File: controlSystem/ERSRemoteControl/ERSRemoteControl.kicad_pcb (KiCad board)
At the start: 2 copper layers, 58.8 x 37.7 mm, 58 parts, among them J1 USB_C_Receptacle_USB2.0_14P, J2 0022-232041, J3 Conn_01x06, J4 00222-32051, J5 0022-232021, J6 0022-232021, SW1 SW_SPDT, SW2 SW_Push, SW3 SW_Push, SW4 SW_Push, SW5 SW_Push, SW6 SW_Push, SW7 SW_Push, U1 TPS63070, U2 ESP32-S3-WROOM-1, U3 TCAN330

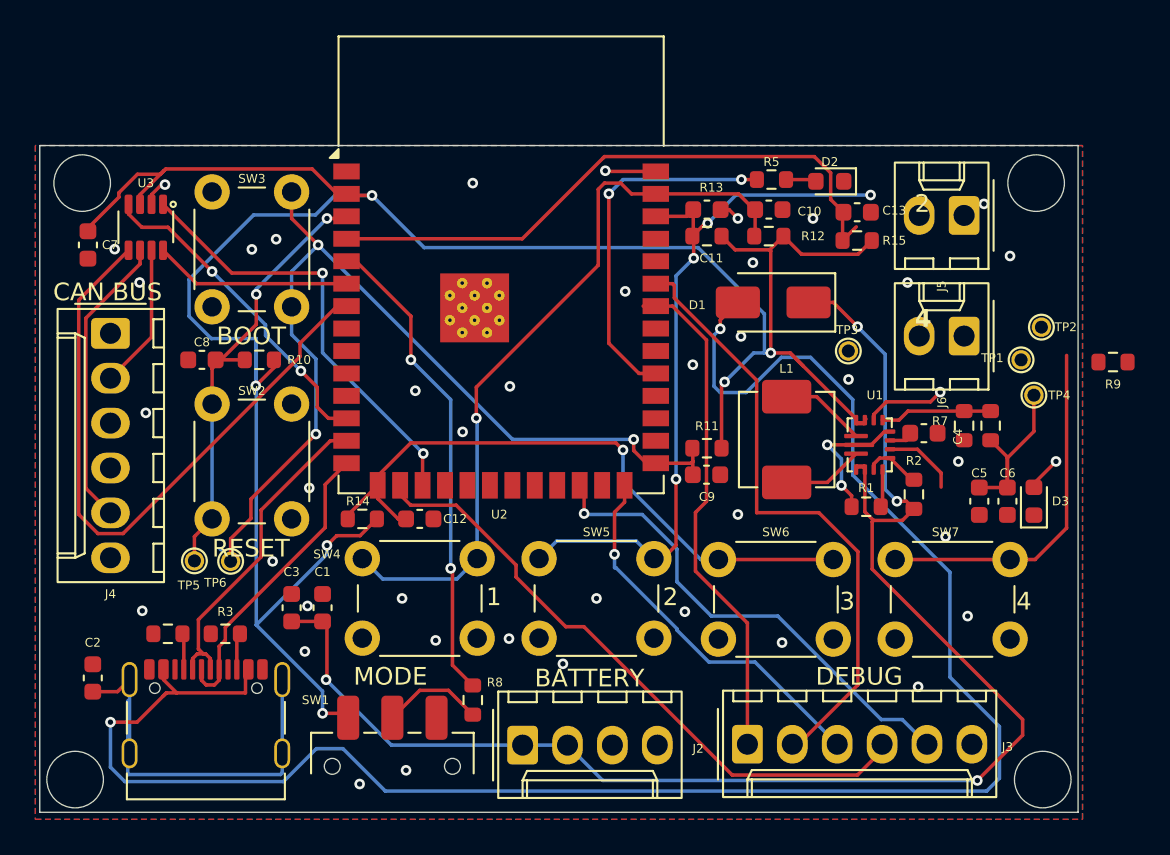
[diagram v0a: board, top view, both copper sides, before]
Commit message: Fixed missing reference designators
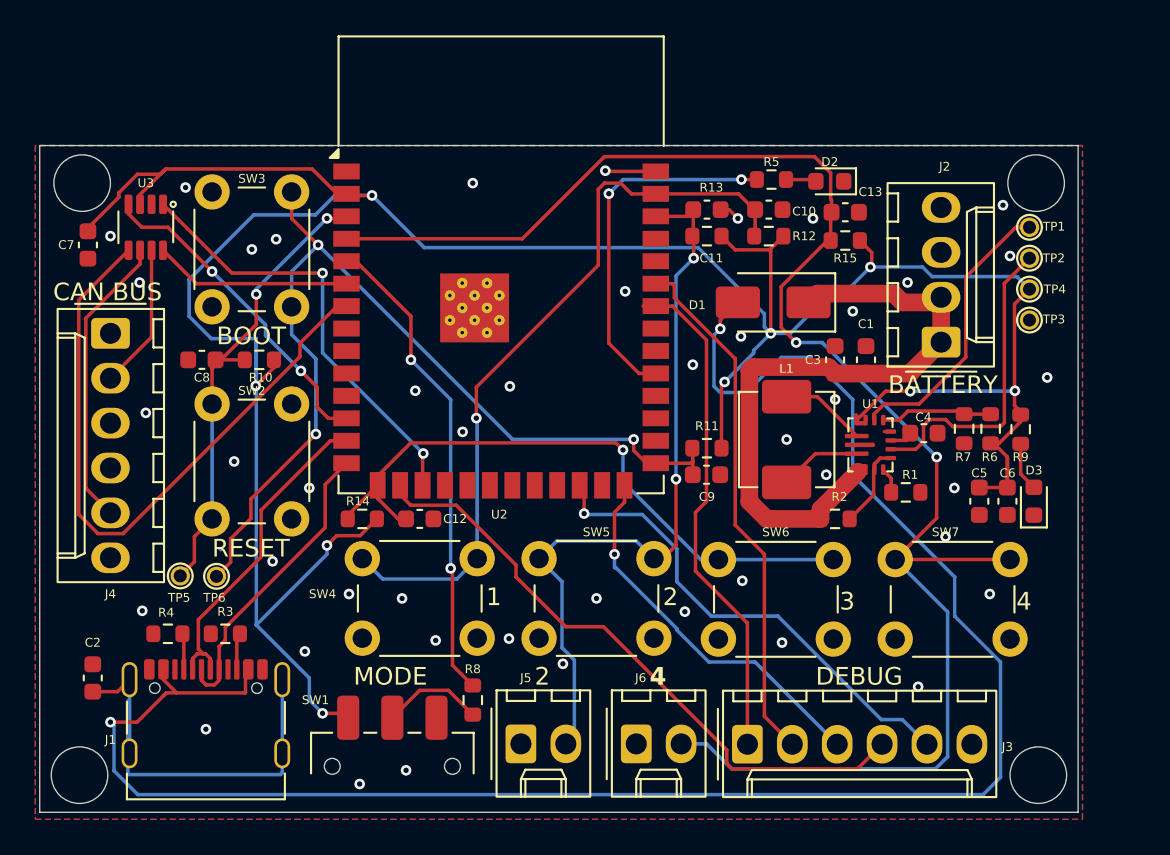
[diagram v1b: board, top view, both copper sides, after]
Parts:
- moved J5 39.0 mm to (101.2, 124.7), turned to 0 degrees
- moved C1 33.8 mm to (120.8, 103.0)
- moved C3 33.8 mm to (119.0, 103.0)
- moved J2 32.9 mm to (125.0, 102.0), turned to 90 degrees
- moved J6 29.6 mm to (107.8, 124.7), turned to 0 degrees
- moved TP3 10.4 mm to (130.0, 100.8)
- moved TP1 7.52 mm to (130.0, 95.5)
- moved R9 6.46 mm to (129.5, 106.9), turned to -90 degrees
- moved TP4 6.01 mm to (130.0, 99.0)
- moved R2 4.67 mm to (119.0, 112.0), turned to 0 degrees
- moved TP2 3.96 mm to (130.0, 97.2)
- moved R1 2.38 mm to (123.0, 110.5), turned to 0 degrees
- moved TP5 1.17 mm to (82.0, 115.2)
- moved TP6 1.17 mm to (84.0, 115.2)
- moved C13 0.67 mm to (119.6, 94.7)
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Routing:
- net Net-(D1-K): track 85.2 -> 37.8 mm, vias 4 -> 0
- net /SWITCH 4: track 55.9 -> 94.0 mm, vias 0 -> 2
- net +3.3V: track 147.0 -> 166.6 mm, vias 6 -> 9
- net Net-(U1-PG): track 4.25 -> 17.8 mm
- net Net-(U1-FB2): track 4.61 -> 16.2 mm, vias 1 -> 0
- net GND: track 14.6 -> 5.57 mm, vias 42 -> 45
- net Net-(J3-Pin_2): track 35.2 -> 30.2 mm
- net Net-(U1-EN): track 3.24 -> 4.75 mm
- net +5V: track 107.0 -> 105.7 mm
- net /BOOT: track 53.2 -> 54.4 mm
- net /RESET: track 26.7 -> 27.9 mm
- net /SWITCH 2: track 41.7 -> 42.8 mm, vias 4 -> 2
- net Net-(D3-A): track 1.98 -> 2.99 mm, vias 1 -> 0
- net Net-(U1-VSEL): track 2.14 -> 1.48 mm

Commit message: Updated traces to .3 instead of .2
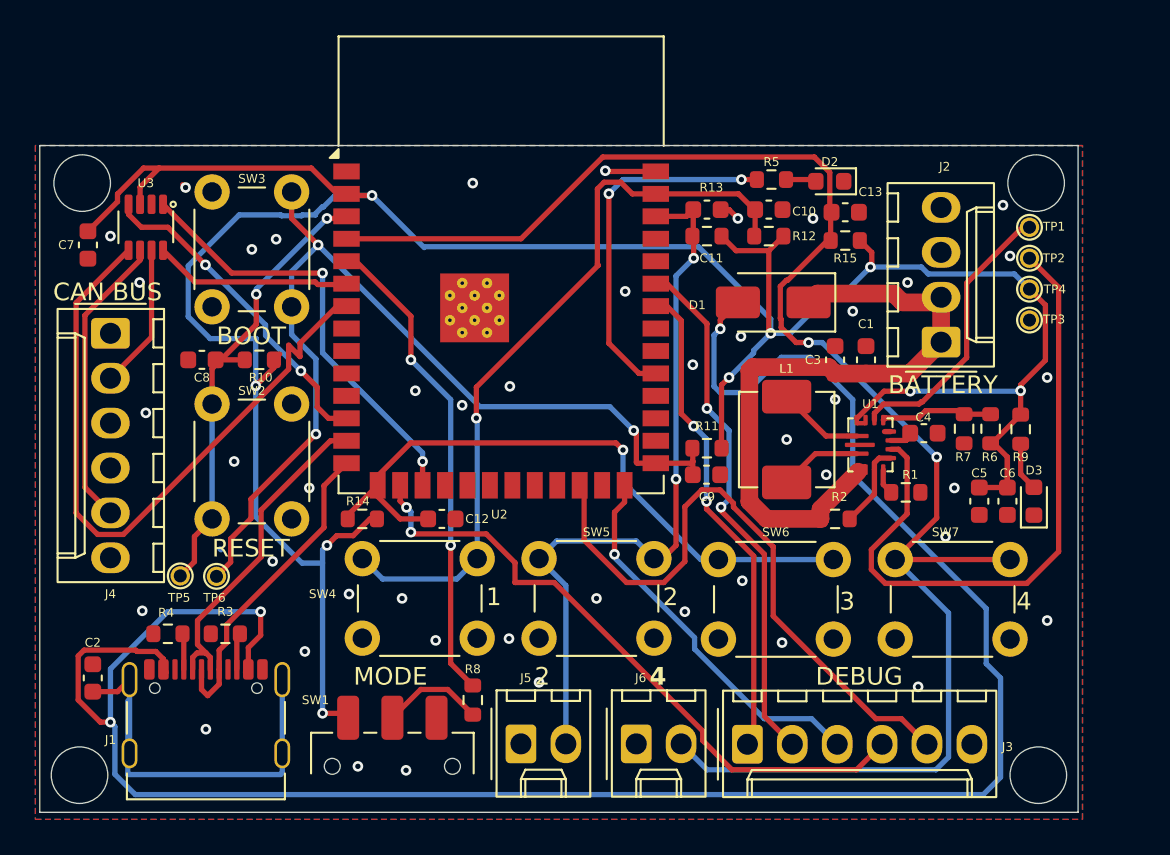
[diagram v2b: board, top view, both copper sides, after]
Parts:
- moved C12 1.25 mm to (96.8, 112.0)
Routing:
- net Net-(U1-PG): track 17.8 -> 37.2 mm
- net +5V: track 105.7 -> 121.4 mm, vias 2 -> 3
- net Net-(J3-Pin_5): track 27.6 -> 36.0 mm, vias 1 -> 0
- net +3.3V: track 166.6 -> 160.6 mm
- net Net-(U2-IO7): track 37.5 -> 39.0 mm
- net /SWITCH 3: track 36.3 -> 37.5 mm
- net Net-(J3-Pin_1): track 28.7 -> 27.6 mm, vias 0 -> 2
- net Net-(J3-Pin_4): track 36.0 -> 37.1 mm, vias 0 -> 2
- net Net-(U2-USB_D+): track 17.1 -> 18.0 mm
- net /BOOT: track 54.4 -> 55.0 mm
- net Net-(J3-Pin_2): track 30.2 -> 30.4 mm, vias 0 -> 2

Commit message: Minor trace updates
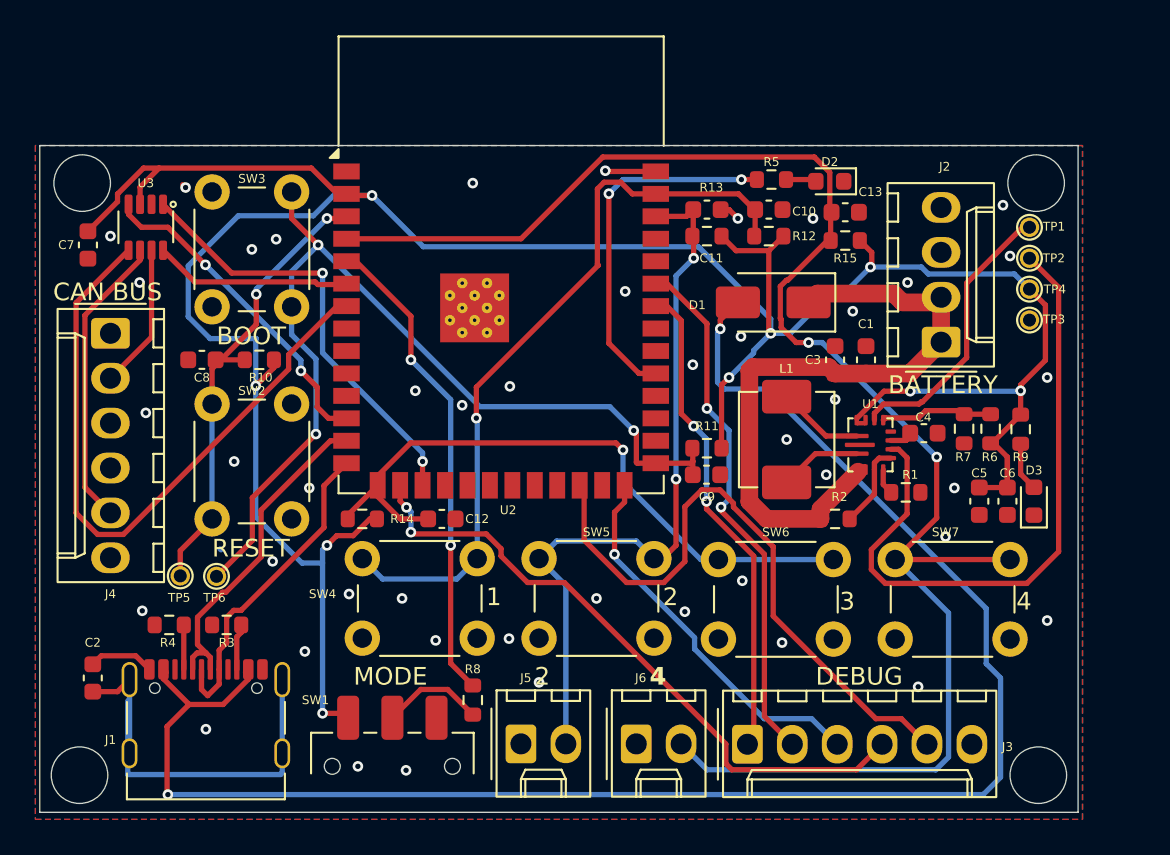
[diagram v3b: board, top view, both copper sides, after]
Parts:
- moved R3 0.51 mm to (84.6, 118.0)
- moved R4 0.51 mm to (81.3, 118.0)
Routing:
- net +5V: track 121.4 -> 96.1 mm, vias 3 -> 2
- net GND: track 5.57 -> 8.93 mm
- net Net-(U2-IO7): track 39.0 -> 37.7 mm
- net Net-(J1-CC2): track 2.09 -> 2.62 mm

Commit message: Removed CAN stuff and replaced with serial
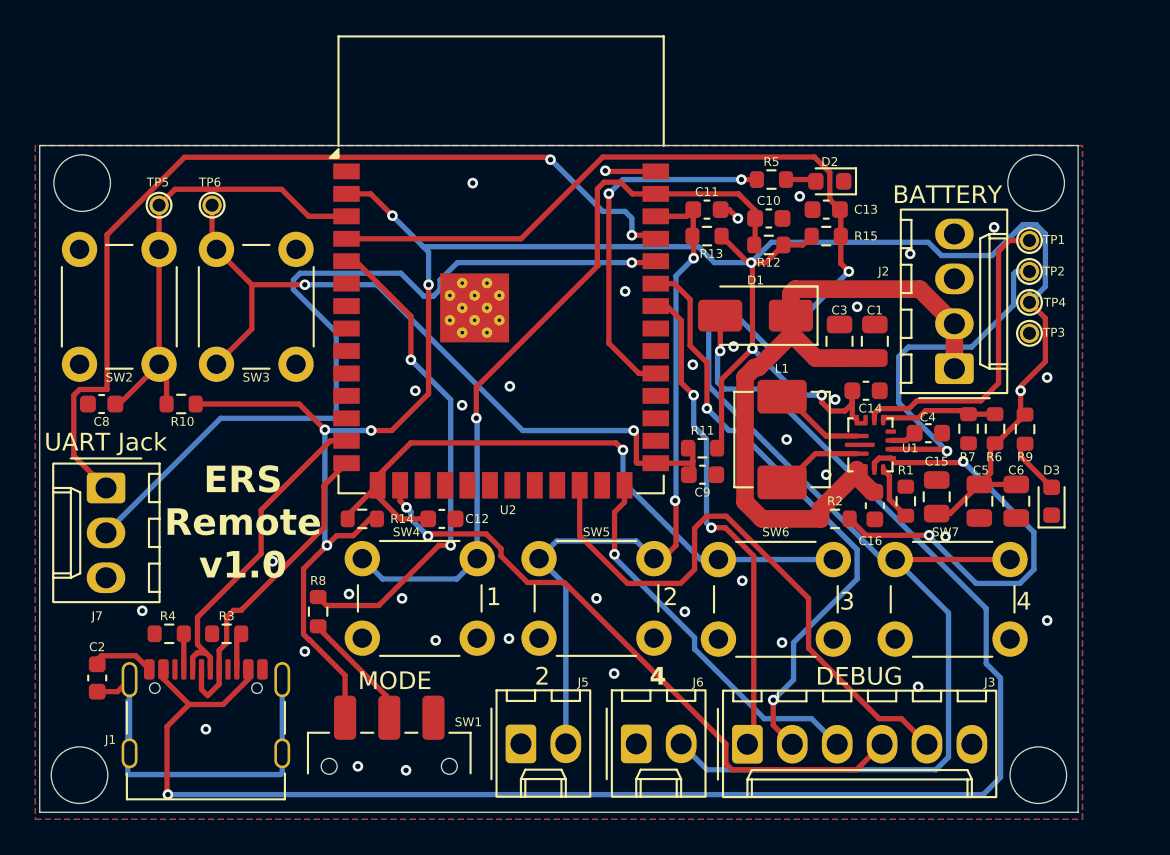
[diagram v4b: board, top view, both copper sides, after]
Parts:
- removed C7: 100n, Capacitor_SMD:C_0603_1608Metric
- removed J4: 00222-32051, Connector_Molex:Molex_KK-254_AE-6410-06A_1x06_P2.54mm_Vertical
- removed U3: TCAN330, psas-footprints:SOT23-8
- added C14: 10u, Capacitor_SMD:C_0603_1608Metric, F.Cu at (120.8, 104.8)
- added C15: 22u, Capacitor_SMD:C_0805_2012Metric, F.Cu at (124.8, 110.8)
- added C16: 10u, Capacitor_SMD:C_0603_1608Metric, F.Cu at (121.2, 111.2)
- added J7: 0022-232031, Connector_Molex:Molex_KK-254_AE-6410-03A_1x03_P2.54mm_Vertical, F.Cu at (77.8, 110.2)
- C1, C3, C5, C6: footprint Capacitor_SMD:C_0603_1608Metric -> Capacitor_SMD:C_0805_2012Metric
- J3: value Conn_01x06 -> 00222-32051
- R5: value 4.7 -> 4.7k
- moved TP5 21.0 mm to (80.8, 94.2)
- moved TP6 21.0 mm to (83.8, 94.2)
- moved SW2 15.5 mm to (80.8, 96.8), turned to -90 degrees
- moved SW3 10.6 mm to (84.0, 103.2), turned to 90 degrees
- moved R8 10.1 mm to (89.8, 117.2)
- moved C8 6.20 mm to (77.5, 105.5)
- moved R10 5.08 mm to (82.0, 105.5)
- moved J2 1.68 mm to (125.8, 103.5)
- moved D1 1.25 mm to (114.5, 100.5)
- moved C1 1.16 mm to (121.2, 102.0)
- moved R15 1.10 mm to (118.5, 96.0), turned to 0 degrees
- moved C13 1.09 mm to (118.5, 94.5), turned to 180 degrees
- moved C3 1.08 mm to (119.2, 102.0)
- moved D3 1.00 mm to (131.2, 111.0)
- moved TP1 0.75 mm to (130.0, 96.2)
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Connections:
- U2 pad 12: Net-(U2-IO8) -> unconnected-(U2-IO8-Pad12)
- U2 pad 17: Net-(U2-IO9) -> unconnected-(U2-IO9-Pad17)
- U2 pad 36: unconnected-(U2-RXD0-Pad36) -> Net-(J7-Pin_2)
- U2 pad 37: unconnected-(U2-TXD0-Pad37) -> Net-(J7-Pin_1)
- U2 pad 6: Net-(U2-IO6) -> unconnected-(U2-IO6-Pad6)
- U2 pad 7: Net-(U2-IO7) -> unconnected-(U2-IO7-Pad7)
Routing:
- net Net-(J7-Pin_1): track 0.00 -> 52.2 mm, vias 0 -> 2
- net Net-(J7-Pin_2): track 0.00 -> 46.9 mm, vias 0 -> 1
- net Net-(U2-IO7): track 37.7 -> 0.00 mm
- net Net-(U2-IO9): track 25.3 -> 0.00 mm, vias 2 -> 0
- net +3.3V: track 160.5 -> 139.0 mm
- net Net-(U1-EN): track 4.79 -> 25.7 mm, vias 0 -> 2
- net Net-(U2-IO8): track 18.7 -> 0.00 mm, vias 2 -> 0
- net Net-(U1-PG): track 37.2 -> 20.1 mm, vias 0 -> 1
- net Net-(J4-Pin_5): track 16.8 -> 0.00 mm
- net /BOOT: track 55.0 -> 42.7 mm, vias 3 -> 2
- net Net-(U2-IO6): track 11.2 -> 0.00 mm
- net Net-(J4-Pin_2): track 8.20 -> 0.00 mm
- net /SWITCH 4: track 94.1 -> 100.1 mm, vias 2 -> 1
- net Net-(J3-Pin_2): track 30.4 -> 34.5 mm
- net Net-(D1-K): track 37.8 -> 41.0 mm
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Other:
- board text added: "ERS Remote v1.0"
- board text added: "UART Jack"
- board text removed: "BOOT"
- board text removed: "CAN BUS"
- board text removed: "RESET"

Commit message: More changes to layout to make it cleaner
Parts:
- removed J3: 00222-32051, Connector_Molex:Molex_KK-254_AE-6410-06A_1x06_P2.54mm_Vertical
- added TP7: Test-Point, psas-footprints:TP-through-hole-1X01, F.Cu at (126.5, 92.0)
- added TP8: Test-Point, psas-footprints:TP-through-hole-1X01, F.Cu at (124.5, 92.0)
- moved J7 20.3 mm to (91.9, 124.8), turned to 0 degrees
- moved J6 15.3 mm to (123.0, 124.8)
- moved J5 14.0 mm to (115.2, 124.7)
- moved SW1 12.9 mm to (106.7, 125.0)
- moved C8 2.12 mm to (79.0, 107.0)
- moved R10 1.50 mm to (82.0, 107.0)
- moved SW2 1.00 mm to (80.8, 97.8)
- moved SW3 1.00 mm to (84.0, 104.2)
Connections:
- U2 pad 16: Net-(J3-Pin_4) -> unconnected-(U2-IO46-Pad16)
- U2 pad 24: Net-(J3-Pin_5) -> unconnected-(U2-IO47-Pad24)
- U2 pad 26: Net-(J3-Pin_3) -> unconnected-(U2-IO45-Pad26)
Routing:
- net Net-(J3-Pin_4): track 36.6 -> 0.00 mm, vias 2 -> 0
- net Net-(J3-Pin_5): track 33.9 -> 0.00 mm
- net Net-(J3-Pin_3): track 21.7 -> 0.00 mm, vias 1 -> 0
- net Net-(SW1-B): track 6.84 -> 26.5 mm
- net Net-(U2-IO42): track 34.5 -> 18.4 mm, vias 2 -> 1
- net Net-(J7-Pin_1): track 52.2 -> 37.0 mm
- net /SWITCH 2: track 43.1 -> 56.2 mm, vias 2 -> 1
- net Net-(J7-Pin_2): track 46.9 -> 36.7 mm, vias 1 -> 2
- net +3.3V: track 139.0 -> 146.7 mm, vias 9 -> 7
- net /SWITCH 4: track 100.1 -> 92.9 mm, vias 1 -> 0
- net Net-(U2-IO41): track 28.1 -> 20.9 mm, vias 2 -> 1
- net Net-(U1-PG): track 20.1 -> 15.4 mm, vias 1 -> 2
- net /RESET: track 27.4 -> 28.6 mm
- net Net-(U1-FB2): track 17.6 -> 16.9 mm, vias 0 -> 1
- net /BOOT: track 42.7 -> 42.4 mm, vias 2 -> 1
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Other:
- board text added: "BOOT"
- board text added: "RESET"
- board text removed: "DEBUG"

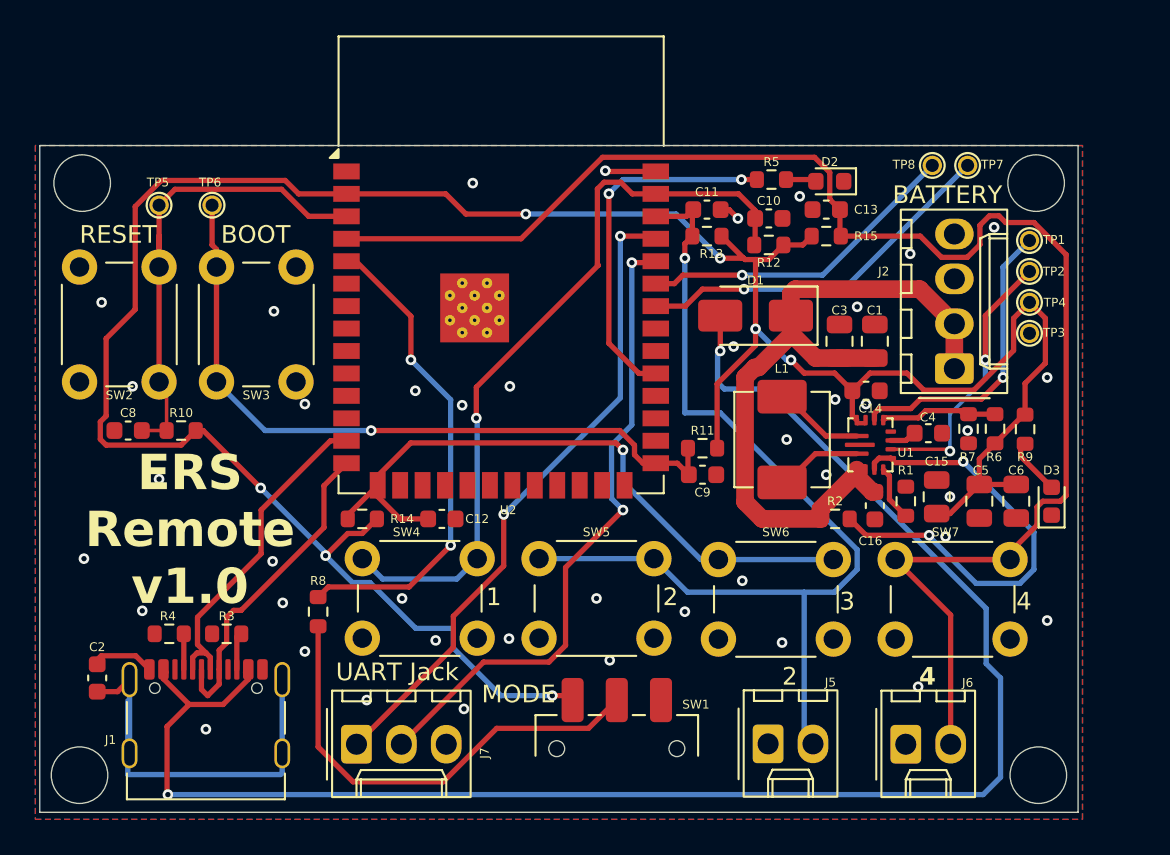
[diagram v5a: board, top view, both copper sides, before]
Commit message: Replaced components in BOM
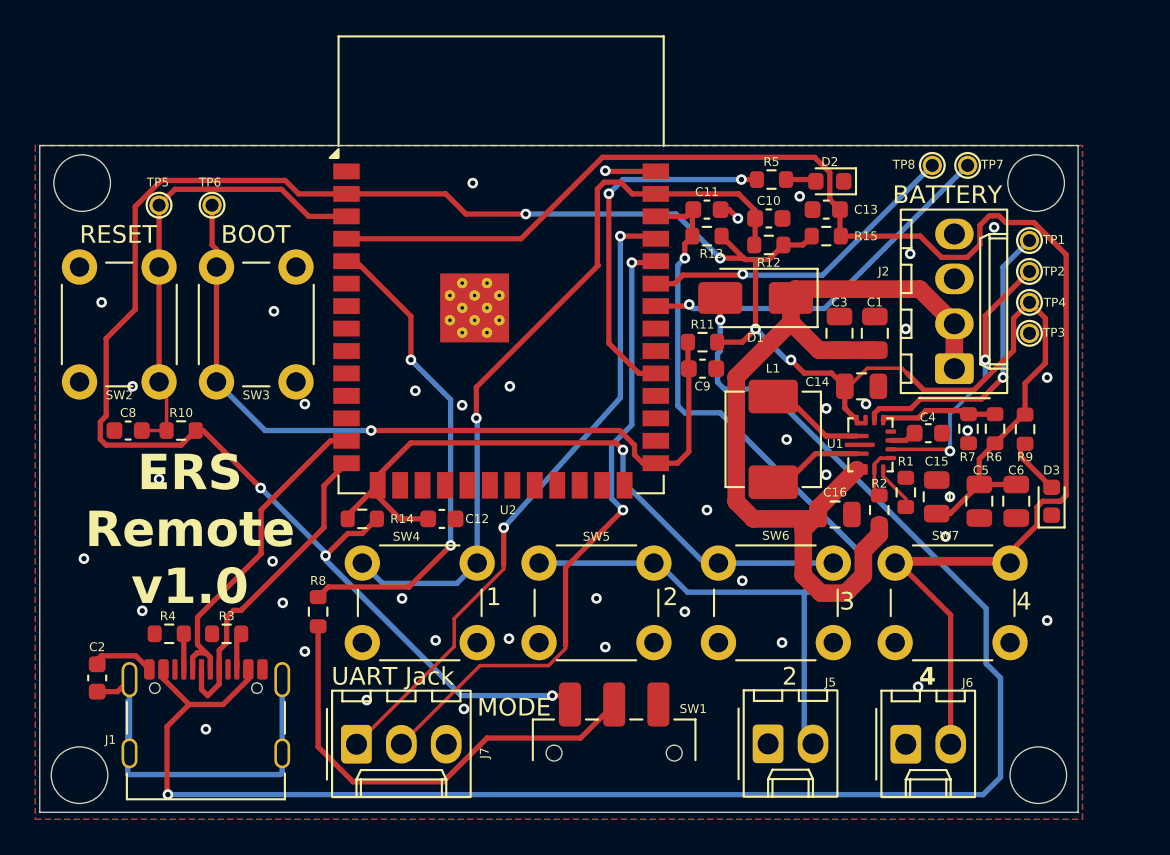
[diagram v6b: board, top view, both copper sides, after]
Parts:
- C14, C16: footprint Capacitor_SMD:C_0603_1608Metric -> Capacitor_SMD:C_0805_2012Metric
- moved C9 6.00 mm to (111.5, 103.5)
- moved R11 6.00 mm to (111.5, 102.0)
- moved R2 2.55 mm to (121.5, 111.5), turned to 90 degrees
- moved C16 2.30 mm to (119.0, 111.8), turned to 0 degrees
- moved D1 1.00 mm to (114.5, 99.5)
- moved L1 0.50 mm to (115.5, 107.5)
- moved R1 0.50 mm to (123.0, 110.5)
- moved C1 0.45 mm to (121.2, 101.5)
- moved C3 0.45 mm to (119.2, 101.5)
- moved C14 0.35 mm to (120.5, 104.5)
- moved SW1 0.29 mm to (106.5, 125.2)
- moved SW4 0.25 mm to (92.2, 114.5)
- moved SW5 0.25 mm to (102.2, 114.5)
- moved SW6 0.20 mm to (112.4, 114.5)
- moved SW7 0.20 mm to (122.4, 114.5)
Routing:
- net Net-(U1-EN): track 25.7 -> 2.96 mm, vias 2 -> 0
- net Net-(D1-K): track 41.0 -> 51.0 mm
- net +3.3V: track 146.7 -> 141.7 mm
- net /BOOT: track 42.4 -> 47.1 mm
- net /RESET: track 28.6 -> 26.9 mm
- net +5V: track 94.9 -> 95.9 mm
- net /SWITCH 2: track 56.2 -> 56.9 mm
- net Net-(U1-L1): track 4.90 -> 5.40 mm
- net Net-(U1-L2): track 5.15 -> 5.65 mm
